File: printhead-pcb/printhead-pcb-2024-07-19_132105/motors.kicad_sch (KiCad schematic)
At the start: 1 part, among them J12 Breakout_Board_ADXL345

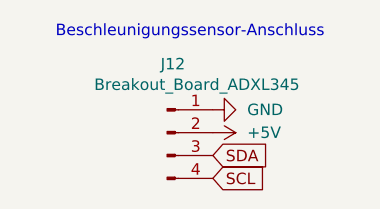
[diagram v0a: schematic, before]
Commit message: made first pcb design of module 1 with components on front and back
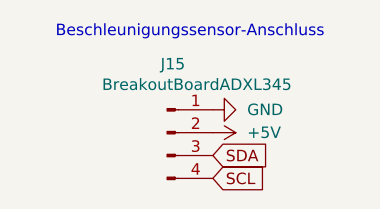
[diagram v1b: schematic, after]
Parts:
- J15: renamed from J12; value Breakout_Board_ADXL345 -> BreakoutBoardADXL345; footprint Connector_PinHeader_2.54mm:PinHeader_1x04_P2.54mm_Horizontal -> Connector_JST:JST_EH_B4B-EH-A_1x04_P2.50mm_Vertical
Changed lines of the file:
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@@
 		(on_board yes)
 		(dnp no)
-		(property "Reference" "J12"
+		(property "Reference" "J15"
 			(at 142.875 41.91 0)
 			(effects
@@
 			)
 		)
-		(property "Value" "Breakout_Board_ADXL345"
+		(property "Value" "BreakoutBoardADXL345"
 			(at 145.542 44.196 0)
 			(effects
@@
 			)
 		)
-		(property "Footprint" "Connector_PinHeader_2.54mm:PinHeader_1x04_P2.54mm_Horizontal"
+		(property "Footprint" "Connector_JST:JST_EH_B4B-EH-A_1x04_P2.50mm_Vertical"
 			(at 142.24 49.53 0)
 			(effects
@@
 			(project "printhead-pcb"
 				(path "/813ad687-b864-44a5-b729-c4edf26b731d/8c761283-af5f-48de-92da-23f77afbf455"
-					(reference "J12")
+					(reference "J15")
 					(unit 1)
 				)
